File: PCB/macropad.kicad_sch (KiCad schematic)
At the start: 11 parts, among them SW10 SW_Push, SW11 SW_Push, SW12 SW_Push, SW2 RotaryEncoder_Switch, SW3 SW_Push, SW4 SW_Push, SW5 SW_Push, SW6 SW_Push, SW7 SW_Push, SW8 SW_Push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

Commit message: Redesign
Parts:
- added D1, D10, D11, D12, D2, D3, D4, D5, D6, D7, D8, D9: 1N4148, Diode_THT:D_DO-35_SOD27_P7.62mm_Horizontal, symbol Diode:1N4148
- added SW1, SW13, SW9: SW_Push, Button_Switch_Keyboard:SW_Cherry_MX_1.00u_PCB, symbol Switch:SW_Push
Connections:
- net GND: now also SW2.S2; no longer SW10.1, SW11.1, SW12.1, SW2.S1, SW3.1, SW4.1, SW5.1, SW6.1, SW7.1, SW8.1
- net at SW6.2: now also D7.2 (A); no longer U1.3 (GPIO28/ADC2/A2)
- net at U1.11 (GPIO3/MOSI): no longer SW12.2
- net at SW2.A: now also U1.9 (GPIO2/SCK); no longer U1.8 (GPIO1/RX)
- net at SW2.B: now also U1.8 (GPIO1/RX); no longer U1.7 (GPIO0/TX)
- net ROW3: now reaches U1.6 (GPIO7/SCL)
- net ROW3: now also D7.1 (K), D8.1 (K), D9.1 (K); no longer SW2.S2
- net at SW3.2: now also D2.2 (A); no longer U1.1 (GPIO26/ADC0/A0)
- net at U1.10 (GPIO4/MISO): now also SW2.S1; no longer SW11.2
- net at U1.12 (3V3): no longer SW8.2
- net at SW5.2: now also D5.2 (A); no longer U1.2 (GPIO27/ADC1/A1)
- net at SW4.2: now also D4.2 (A); no longer U1.4 (GPIO29/ADC3/A3)
- net at SW7.2: now also D8.2 (A); no longer U1.5 (GPIO6/SDA)
- net at SW10.2: now also D3.2 (A); no longer U1.9 (GPIO2/SCK)
- new net: D11.2 (A), SW9.2
- new net: D1.2 (A), SW1.2
- new net: D6.2 (A), SW11.2
- new net: D9.2 (A), SW12.2
- new net: D10.2 (A), SW8.2
- new net: D12.2 (A), SW13.2
- new net COL1: SW1.1, SW4.1, SW6.1, SW8.1, U1.1 (GPIO26/ADC0/A0)
- new net COL2: SW3.1, SW5.1, SW7.1, SW9.1, U1.2 (GPIO27/ADC1/A1)
- new net COL3: SW10.1, SW11.1, SW12.1, SW13.1, U1.3 (GPIO28/ADC2/A2)
- new net ROW1: D1.1 (K), D2.1 (K), D3.1 (K), U1.4 (GPIO29/ADC3/A3)
- new net ROW2: D4.1 (K), D5.1 (K), D6.1 (K), U1.5 (GPIO6/SDA)
- new net ROW4: D10.1 (K), D11.1 (K), D12.1 (K), U1.7 (GPIO0/TX)
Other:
- moved on the sheet: SW2

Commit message: update
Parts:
- added D13, D14, D15: 1N4148, Diode_THT:D_DO-35_SOD27_P7.62mm_Horizontal, symbol Diode:1N4148
- added SW14, SW15, SW16: SW_Push, Button_Switch_Keyboard:SW_Cherry_MX_1.00u_PCB, symbol Switch:SW_Push
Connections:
- net ROW1: now also D13.1 (K)
- net ROW2: now also D14.1 (K)
- net ROW3: now also D15.1 (K)
- net COL4: now reaches U1.11 (GPIO3/MOSI)
- net COL4: now also SW14.1, SW15.1, SW16.1
- new net: D15.2 (A), SW16.2
- new net: D13.2 (A), SW14.2
- new net: D14.2 (A), SW15.2

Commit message: Add files via upload
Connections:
- net ROW3: now also U1.7 (GPIO0/TX); no longer U1.6 (GPIO7/SCL)
- net ROW4: now also U1.6 (GPIO7/SCL); no longer U1.7 (GPIO0/TX)
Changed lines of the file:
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@@
 		)
 	)
-	(global_label "ROW4"
+	(global_label "ROW3"
 		(shape input)
 		(at 119.38 130.81 180)
@@
 		)
 	)
-	(global_label "ROW3"
+	(global_label "ROW4"
 		(shape input)
 		(at 119.38 127 180)

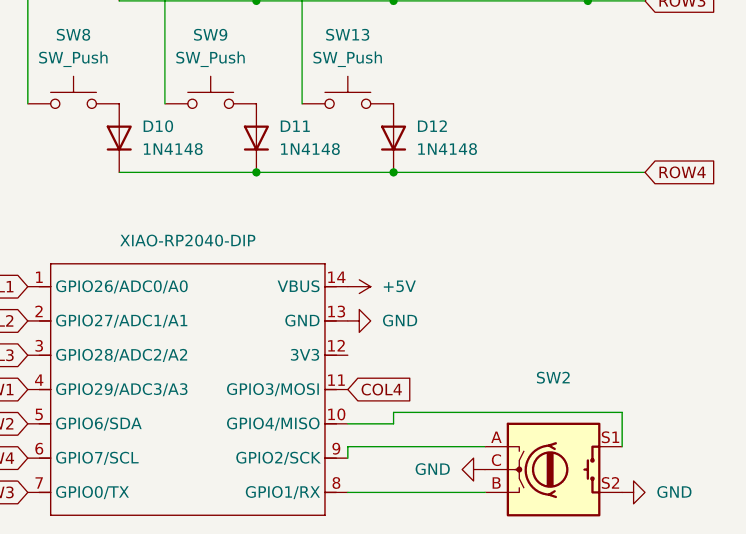
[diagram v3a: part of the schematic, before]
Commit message: Added vias for ground plane
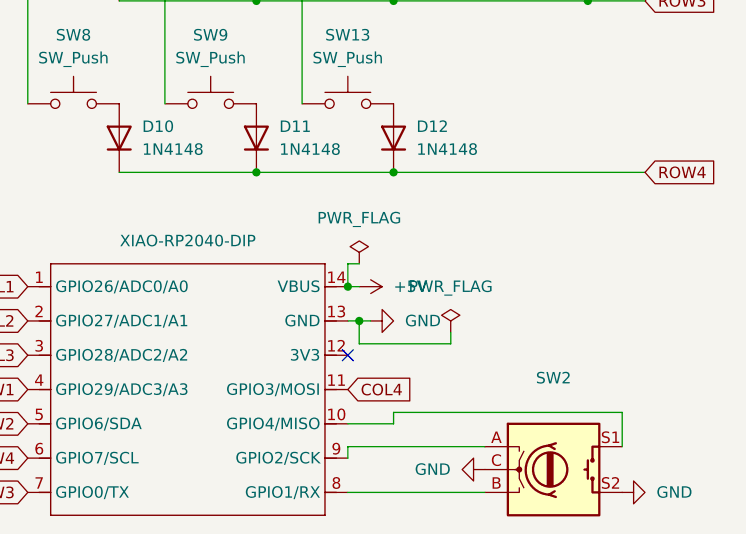
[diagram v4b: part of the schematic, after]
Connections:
- no-connect marks 0 -> 1
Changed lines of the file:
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@@
 	)
 	(junction
+		(at 154.94 107.95)
+		(diameter 0)
+		(color 0 0 0 0)
+	)
+	(junction
 		(at 160.02 95.25)
 		(diameter 0)
@@
 	)
 	(junction
+		(at 156.21 111.76)
+		(diameter 0)
+		(color 0 0 0 0)
+	)
+	(junction
 		(at 134.62 33.02)
 		(diameter 0)
@@
 		(color 0 0 0 0)
 	)
+	(no_connect
+		(at 154.94 115.57)
+	)
+	(wire
+		(pts
+			(xy 156.21 111.76) (xy 154.94 111.76)
+		)
+		(stroke
+			(width 0)
+			(type default)
+		)
+	)
 	(wire
 		(pts
@@
 	(wire
 		(pts
+			(xy 156.21 107.95) (xy 154.94 107.95)
+		)
+		(stroke
+			(width 0)
+			(type default)
+		)
+	)
+	(wire
+		(pts
 			(xy 170.18 125.73) (xy 154.94 125.73)
 		)
@@
 	(wire
 		(pts
+			(xy 157.48 111.76) (xy 156.21 111.76)
+		)
+		(stroke
+			(width 0)
+			(type default)
+		)
+	)
+	(wire
+		(pts
 			(xy 185.42 125.73) (xy 185.42 121.92)
 		)
@@
 	(wire
 		(pts
+			(xy 166.37 113.03) (xy 166.37 114.3)
+		)
+		(stroke
+			(width 0)
+			(type default)
+		)
+	)
+	(wire
+		(pts
+			(xy 156.21 114.3) (xy 156.21 111.76)
+		)
+		(stroke
+			(width 0)
+			(type default)
+		)
+	)
+	(wire
+		(pts
 			(xy 129.54 58.42) (xy 144.78 58.42)
 		)
@@
 	(wire
 		(pts
+			(xy 154.94 105.41) (xy 154.94 107.95)
+		)
+		(stroke
+			(width 0)
+			(type default)
+		)
+	)
+	(wire
+		(pts
 			(xy 134.62 50.8) (xy 134.62 68.58)
 		)
@@
 	(wire
 		(pts
+			(xy 154.94 105.41) (xy 156.21 105.41)
+		)
+		(stroke
+			(width 0)
+			(type default)
+		)
+	)
+	(wire
+		(pts
 			(xy 119.38 68.58) (xy 119.38 87.63)
 		)
@@
 	(wire
 		(pts
+			(xy 166.37 114.3) (xy 156.21 114.3)
+		)
+		(stroke
+			(width 0)
+			(type default)
+		)
+	)
+	(wire
+		(pts
 			(xy 149.86 33.02) (xy 149.86 50.8)
 		)
@@
 	(symbol
 		(lib_id "power:GND")
-		(at 154.94 111.76 90)
+		(at 157.48 111.76 90)
 		(unit 1)
 		(exclude_from_sim no)
@@
 		(fields_autoplaced yes)
 		(property "Reference" "#PWR02"
-			(at 161.29 111.76 0)
+			(at 163.83 111.76 0)
 			(effects
 				(font
@@
 		)
 		(property "Value" "GND"
-			(at 158.75 111.7599 90)
+			(at 161.29 111.7599 90)
 			(effects
 				(font
@@
 		)
 		(property "Footprint" ""
-			(at 154.94 111.76 0)
+			(at 157.48 111.76 0)
 			(effects
 				(font
@@
 		)
 		(property "Datasheet" ""
-			(at 154.94 111.76 0)
+			(at 157.48 111.76 0)
 			(effects
 				(font
@@
 		)
 		(property "Description" "Power symbol creates a global label with name \"GND\" , ground"
-			(at 154.94 111.76 0)
+			(at 157.48 111.76 0)
 			(effects
 				(font
@@
 	)
 	(symbol
+		(lib_id "power:PWR_FLAG")
+		(at 166.37 113.03 0)
+		(unit 1)
+		(exclude_from_sim no)
+		(in_bom yes)
+		(on_board yes)
+		(dnp no)
+		(fields_autoplaced yes)
+		(property "Reference" "#FLG02"
+			(at 166.37 111.125 0)
+			(effects
+				(font
+					(size 1.27 1.27)
+				)
+				(hide yes)
+			)
+		)
+		(property "Value" "PWR_FLAG"
+			(at 166.37 107.95 0)
+			(effects
+				(font
+					(size 1.27 1.27)
+				)
+			)
+		)
+		(property "Footprint" ""
+			(at 166.37 113.03 0)
+			(effects
+				(font
+					(size 1.27 1.27)
+				)
+				(hide yes)
+			)
+		)
+		(property "Datasheet" "~"
+			(at 166.37 113.03 0)
+			(effects
+				(font
+					(size 1.27 1.27)
+				)
+				(hide yes)
+			)
+		)
+		(property "Description" "Special symbol for telling ERC where power comes from"
+			(at 166.37 113.03 0)
+			(effects
+				(font
+					(size 1.27 1.27)
+				)
+				(hide yes)
+			)
+		)
+		(pin "1"
+		)
+		(instances
+			(project "macropad"
+				(path "/c1defd57-51fe-4569-9e13-a5ca4d7f48a3"
+					(reference "#FLG02")
+					(unit 1)
+				)
+			)
+		)
+	)
+	(symbol
 		(lib_id "Diode:1N4148")
 		(at 160.02 72.39 90)
@@
 	)
 	(symbol
+		(lib_id "power:PWR_FLAG")
+		(at 156.21 105.41 0)
+		(unit 1)
+		(exclude_from_sim no)
+		(in_bom yes)
+		(on_board yes)
+		(dnp no)
+		(fields_autoplaced yes)
+		(property "Reference" "#FLG01"
+			(at 156.21 103.505 0)
+			(effects
+				(font
+					(size 1.27 1.27)
+				)
+				(hide yes)
+			)
+		)
+		(property "Value" "PWR_FLAG"
+			(at 156.21 100.33 0)
+			(effects
+				(font
+					(size 1.27 1.27)
+				)
+			)
+		)
+		(property "Footprint" ""
+			(at 156.21 105.41 0)
+			(effects
+				(font
+					(size 1.27 1.27)
+				)
+				(hide yes)
+			)
+		)
+		(property "Datasheet" "~"
+			(at 156.21 105.41 0)
+			(effects
+				(font
+					(size 1.27 1.27)
+				)
+				(hide yes)
+			)
+		)
+		(property "Description" "Special symbol for telling ERC where power comes from"
+			(at 156.21 105.41 0)
+			(effects
+				(font
+					(size 1.27 1.27)
+				)
+				(hide yes)
+			)
+		)
+		(pin "1"
+		)
+		(instances
+			(project ""
+				(path "/c1defd57-51fe-4569-9e13-a5ca4d7f48a3"
+					(reference "#FLG01")
+					(unit 1)
+				)
+			)
+		)
+	)
+	(symbol
 		(lib_id "Switch:SW_Push")
 		(at 176.53 33.02 0)
@@
 	(symbol
 		(lib_id "power:+5V")
-		(at 154.94 107.95 270)
+		(at 156.21 107.95 270)
 		(unit 1)
 		(exclude_from_sim no)
@@
 		(fields_autoplaced yes)
 		(property "Reference" "#PWR01"
-			(at 151.13 107.95 0)
+			(at 152.4 107.95 0)
 			(effects
 				(font
@@
 		)
 		(property "Value" "+5V"
-			(at 158.75 107.9499 90)
+			(at 160.02 107.9499 90)
 			(effects
 				(font
@@
 		)
 		(property "Footprint" ""
-			(at 154.94 107.95 0)
+			(at 156.21 107.95 0)
 			(effects
 				(font
@@
 		)
 		(property "Datasheet" ""
-			(at 154.94 107.95 0)
+			(at 156.21 107.95 0)
 			(effects
 				(font
@@
 		)
 		(property "Description" "Power symbol creates a global label with name \"+5V\""
-			(at 154.94 107.95 0)
+			(at 156.21 107.95 0)
 			(effects
 				(font
